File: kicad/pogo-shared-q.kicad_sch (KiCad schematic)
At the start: 8 parts, among them U10 LM13700, U9 LM13700

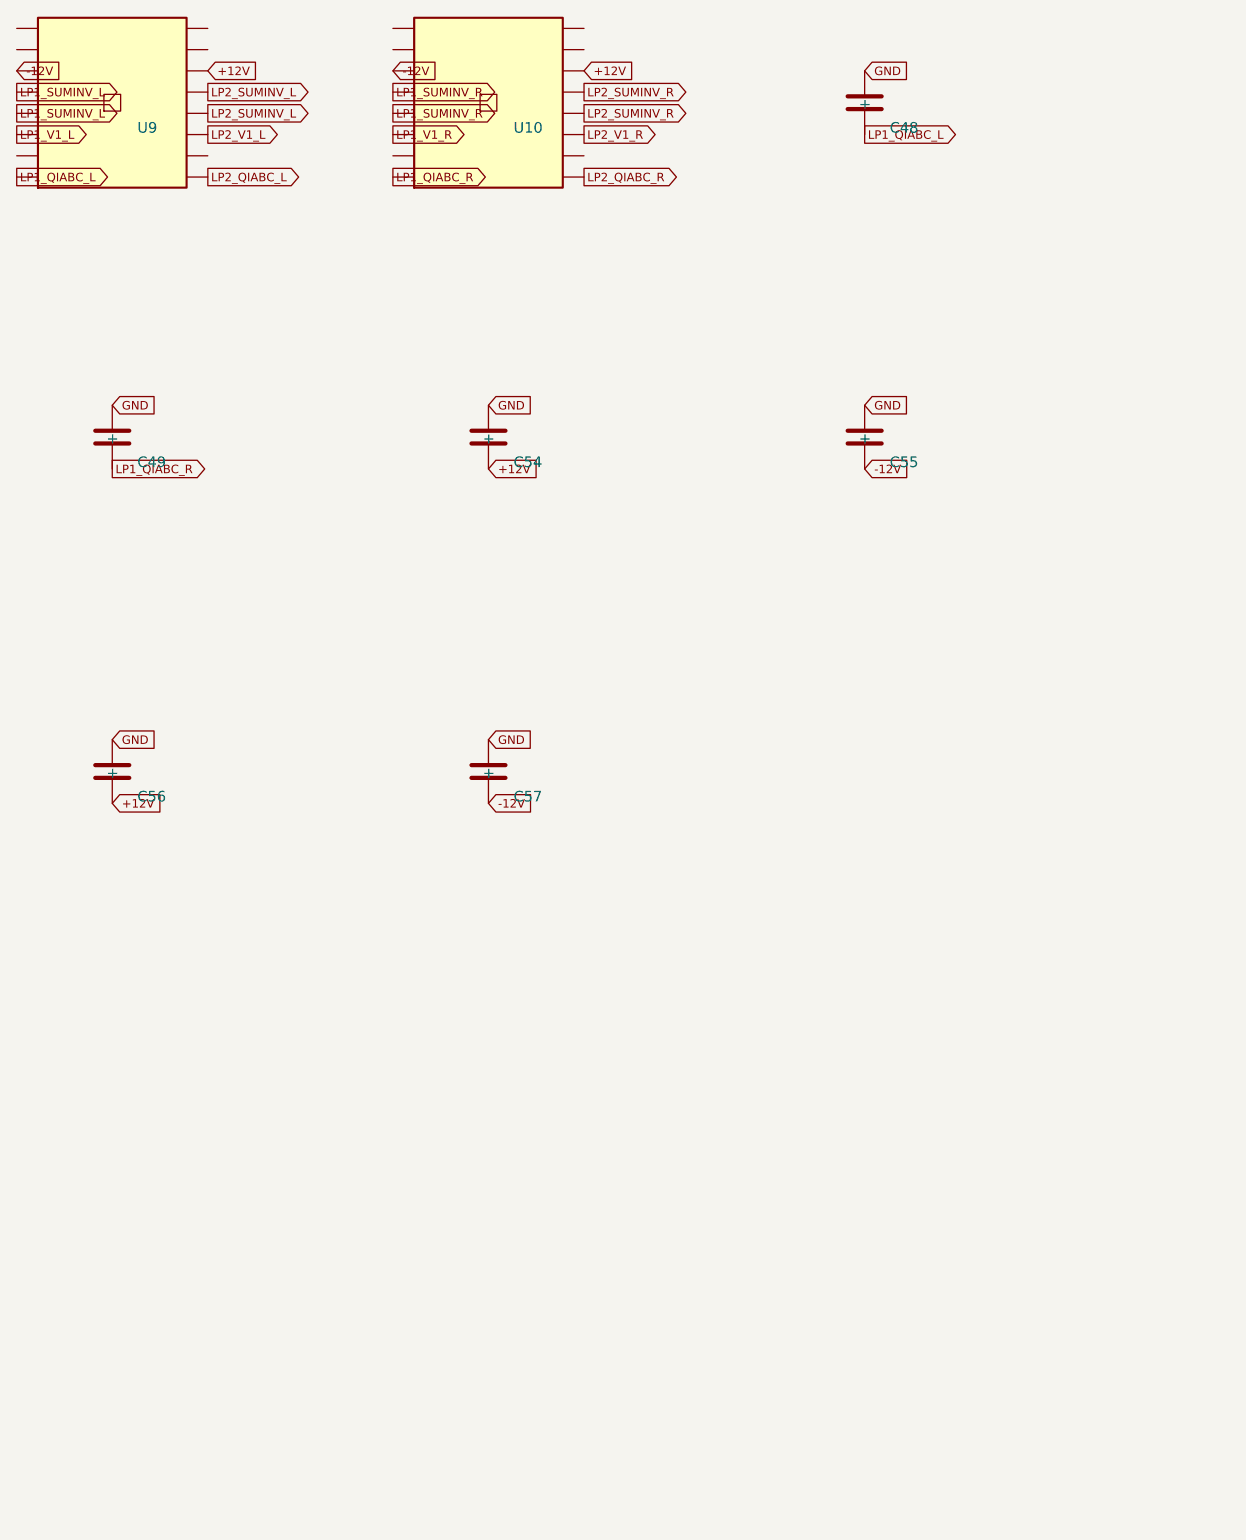
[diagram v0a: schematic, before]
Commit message: kicad: block-8 LP2 + fix multi-unit op-amp placement bug (7 of 10)
block-8 (LP2): OTA-C SVF mirroring LP1 minus tilt (single shared expo); Q VCA via
the shared-q sheet cell B (U9/U10); added LP2's own IRES_AMP (U65, was missing from
the BOM) + full SVF expansion (R_LIN, expo network, Q V->I, buffer pulldowns,
decoupling). 51 parts / 36 nets; LP2 boundary nets match shared-q byte-for-byte.
shared-q gains the LP2 cell-B Iabc bypass caps (C84/C85).

GENERATOR CORRECTNESS FIX (exposed by block-8's spare op-amp half): dual op-amps
were placed as a single instance while pins from BOTH halves were connected at the
lib_symbol's overlapping origin -> unit-A and unit-B pins landed on the same canvas
point, shorting the two halves. This was latent in EVERY dual-op-amp block (A,B,1,2,
4,5). Fix:
- place each gate unit (A/B/power) as its own instance at distinct offsets
  (MULTI_UNIT + opamp_unit_pins);
- make structural_check unit-aware (per-sub-symbol unit pins);
- add a short detector: 2+ distinct nets whose labels coincide at one point now fail.
All blocks regenerated and re-verified clean (the detector finds no shorts).

STATUS+plan: 7/10 blocks. All gates green.
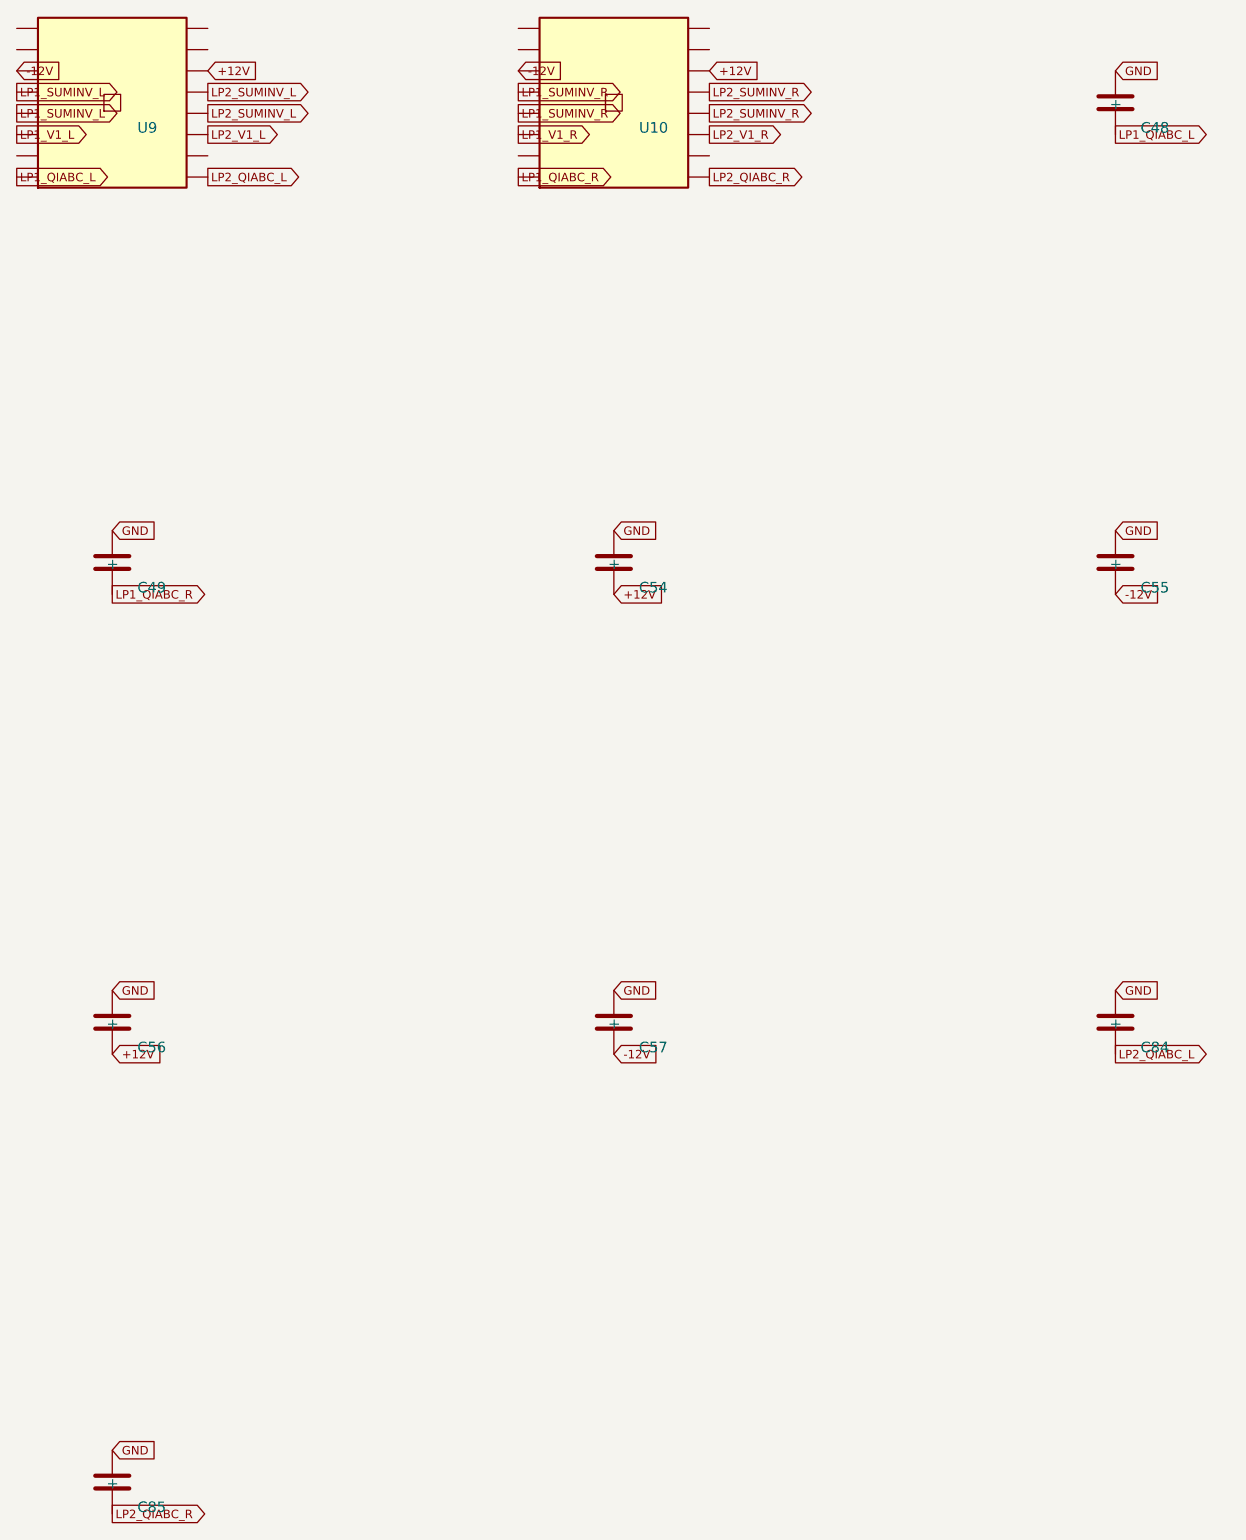
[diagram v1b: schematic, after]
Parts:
- added C84, C85: 10nF, symbol Device:C
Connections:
- net GND: now also C84.1 (+), C85.1 (+)
- net LP2_QIABC_L: now also C84.2
- net LP2_QIABC_R: now also C85.2
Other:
- moved on the sheet: C48, C49, C54, C55, C56, C57, U10
